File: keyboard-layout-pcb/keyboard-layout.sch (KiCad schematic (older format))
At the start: 33 parts, among them J1 Conn_01x06, J2 Conn_01x02, J3 Conn_01x02, Q1 IRLB871, U1 TSOP384xx, U2 TSMP58000, U3 RFM9xLoRa

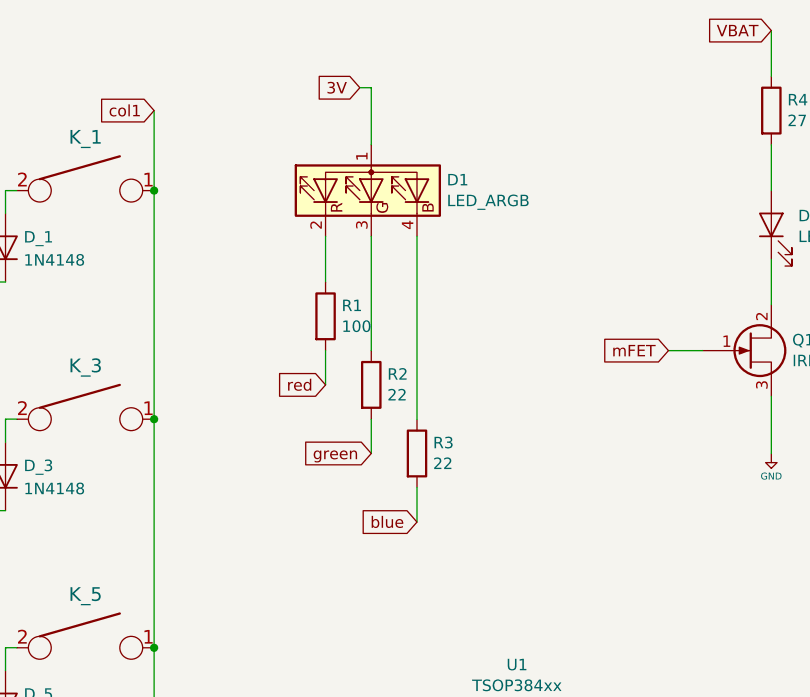
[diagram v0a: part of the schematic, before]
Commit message: Updated scematic to releft current operation
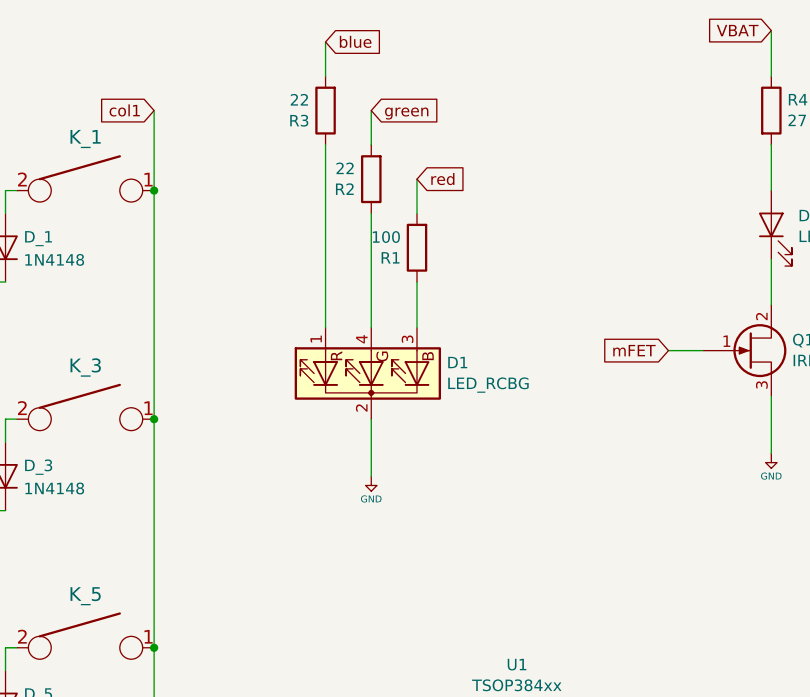
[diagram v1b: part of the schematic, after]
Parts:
- removed D1: LED_ARGB, LEDs:LED_D5.0mm-4, symbol Device:LED_ARGB
- added D1: LED_RCBG, LED_THT:LED_D5.0mm-4_RGB, symbol Device:LED_RCBG
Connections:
- net +5V: now also D1.2 (K)
- net at R1.1: now also D1.3 (BA)
- net at R2.1: now also D1.4 (GA)
- net at R3.1: now also D1.1 (RA)
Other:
- moved on the sheet: R1, R2, R3
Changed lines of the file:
@@
 	5250 5500 5400 5500
-$Comp
-L Device:LED_ARGB D1
-U 1 1 5DB4EFC4
-P 4250 2000
-F 0 "D1" V 4296 1670 50  0000 R CNN
-F 1 "LED_ARGB" V 4205 1670 50  0000 R CNN
-F 2 "LEDs:LED_D5.0mm-4" H 4250 1950 50  0001 C CNN
-F 3 "~" H 4250 1950 50  0001 C CNN
-	1    4250 2000
-	0    -1   -1   0
-$EndComp
 $Comp
 L Device:R R1
 U 1 1 5DB5148C
-P 4050 2550
-F 0 "R1" H 4120 2596 50  0000 L CNN
-F 1 "100" H 4120 2505 50  0000 L CNN
-F 2 "Resistors_THT:R_Axial_DIN0411_L9.9mm_D3.6mm_P12.70mm_Horizontal" V 3980 2550 50  0001 C CNN
-F 3 "~" H 4050 2550 50  0001 C CNN
-	1    4050 2550
-	1    0    0    -1
+P 4450 2250
+F 0 "R1" H 4520 2296 50  0000 L CNN
+F 1 "100" H 4520 2205 50  0000 L CNN
+F 2 "Resistors_THT:R_Axial_DIN0411_L9.9mm_D3.6mm_P12.70mm_Horizontal" V 4380 2250 50  0001 C CNN
+F 3 "~" H 4450 2250 50  0001 C CNN
+	1    4450 2250
+	-1   0    0    1
 $EndComp
 $Comp
 L Device:R R2
 U 1 1 5DB51AFC
-P 4250 2850
-F 0 "R2" H 4320 2896 50  0000 L CNN
-F 1 "22" H 4320 2805 50  0000 L CNN
-F 2 "Resistors_THT:R_Axial_DIN0411_L9.9mm_D3.6mm_P12.70mm_Horizontal" V 4180 2850 50  0001 C CNN
-F 3 "~" H 4250 2850 50  0001 C CNN
-	1    4250 2850
-	1    0    0    -1
+P 4250 1950
+F 0 "R2" H 4320 1996 50  0000 L CNN
+F 1 "22" H 4320 1905 50  0000 L CNN
+F 2 "Resistors_THT:R_Axial_DIN0411_L9.9mm_D3.6mm_P12.70mm_Horizontal" V 4180 1950 50  0001 C CNN
+F 3 "~" H 4250 1950 50  0001 C CNN
+	1    4250 1950
+	-1   0    0    1
 $EndComp
 $Comp
 L Device:R R3
 U 1 1 5DB51F49
-P 4450 3150
-F 0 "R3" H 4520 3196 50  0000 L CNN
-F 1 "22" H 4520 3105 50  0000 L CNN
-F 2 "Resistors_THT:R_Axial_DIN0411_L9.9mm_D3.6mm_P12.70mm_Horizontal" V 4380 3150 50  0001 C CNN
-F 3 "~" H 4450 3150 50  0001 C CNN
-	1    4450 3150
-	1    0    0    -1
-$EndComp
-Text GLabel 4050 2850 0    50   Input ~ 0
+P 4050 1650
+F 0 "R3" H 4120 1696 50  0000 L CNN
+F 1 "22" H 4120 1605 50  0000 L CNN
+F 2 "Resistors_THT:R_Axial_DIN0411_L9.9mm_D3.6mm_P12.70mm_Horizontal" V 3980 1650 50  0001 C CNN
+F 3 "~" H 4050 1650 50  0001 C CNN
+	1    4050 1650
+	-1   0    0    1
+$EndComp
+Text GLabel 4450 1950 2    50   Input ~ 0
 red
-Text GLabel 4250 3150 0    50   Input ~ 0
+Text GLabel 4250 1650 2    50   Input ~ 0
 green
-Text GLabel 4450 3450 0    50   Input ~ 0
+Text GLabel 4050 1350 2    50   Input ~ 0
 blue
 Wire Wire Line
-	4050 2400 4050 2200
-Wire Wire Line
-	4250 2200 4250 2700
-Wire Wire Line
-	4450 2200 4450 3000
-Wire Wire Line
-	4250 3000 4250 3150
-Wire Wire Line
-	4050 2700 4050 2850
-Wire Wire Line
-	4450 3300 4450 3450
+	4450 2400 4450 2600
+Wire Wire Line
+	4250 2600 4250 2100
+Wire Wire Line
+	4050 2600 4050 1800
+Wire Wire Line
+	4250 1800 4250 1650
+Wire Wire Line
+	4450 2100 4450 1950
+Wire Wire Line
+	4050 1500 4050 1350
 Text GLabel 7950 2950 0    50   Input ~ 0
 row0
@@
 Wire Wire Line
 	7950 2650 8100 2650
-Text GLabel 4200 1550 0    50   Input ~ 0
-3V
-Wire Wire Line
-	4200 1550 4250 1550
-Wire Wire Line
-	4250 1550 4250 1800
+Wire Wire Line
+	4250 3250 4250 3000
 Text GLabel 5400 5300 2    50   Input ~ 0
 3V
@@
 Wire Wire Line
 	5450 4300 5300 4300
+$Comp
+L keyboard_parts:GND #PWR01
+U 1 1 5DEEC9A8
+P 4250 3250
+F 0 "#PWR01" H 4250 3300 20  0001 C CNN
+F 1 "GND" H 4250 3150 30  0000 C CNN
+F 2 "" H 4250 3250 60  0000 C CNN
+F 3 "" H 4250 3250 60  0000 C CNN
+	1    4250 3250
+	1    0    0    -1
+$EndComp
+$Comp
+L Device:LED_RCBG D1
+U 1 1 5DEFA295
+P 4250 2800
+F 0 "D1" V 4296 2470 50  0000 R CNN
+F 1 "LED_RCBG" V 4205 2470 50  0000 R CNN
+F 2 "LED_THT:LED_D5.0mm-4_RGB" H 4250 2750 50  0001 C CNN
+F 3 "~" H 4250 2750 50  0001 C CNN
+	1    4250 2800
+	0    -1   -1   0
+$EndComp
 $EndSCHEMATC

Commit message: Revert "Updated scematic to releft current operation"
This reverts commit bc39922ebd05a59e5cfd160ddaddfcfa669e5cef.
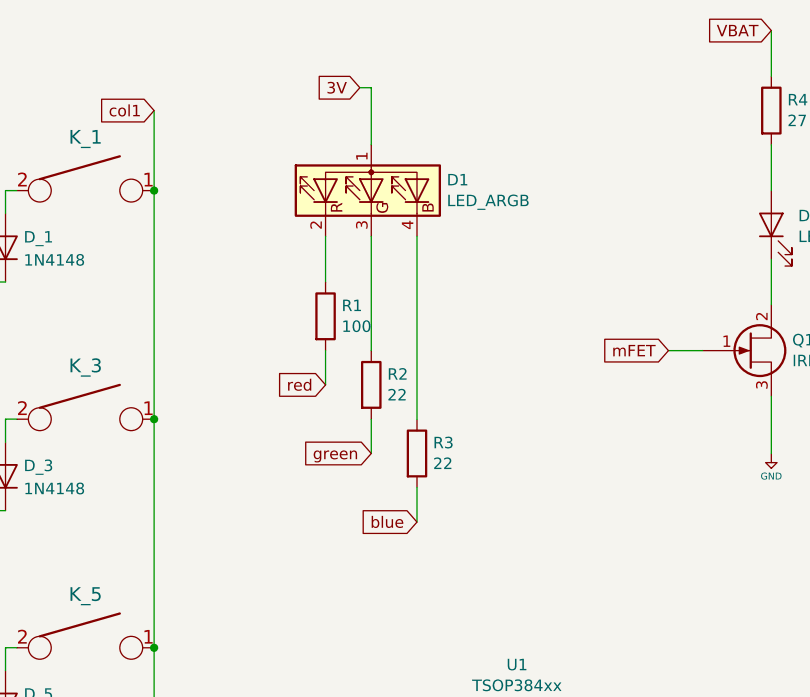
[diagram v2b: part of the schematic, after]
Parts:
- removed D1: LED_RCBG, LED_THT:LED_D5.0mm-4_RGB, symbol Device:LED_RCBG
- added D1: LED_ARGB, LEDs:LED_D5.0mm-4, symbol Device:LED_ARGB
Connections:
- net 3V: now also D1.1 (A)
- net at R1.1: now also D1.2 (RK)
- net at R2.1: now also D1.3 (GK)
- net at R3.1: now also D1.4 (BK)
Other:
- moved on the sheet: R1, R2, R3
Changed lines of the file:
@@
 	5250 5500 5400 5500
+$Comp
+L Device:LED_ARGB D1
+U 1 1 5DB4EFC4
+P 4250 2000
+F 0 "D1" V 4296 1670 50  0000 R CNN
+F 1 "LED_ARGB" V 4205 1670 50  0000 R CNN
+F 2 "LEDs:LED_D5.0mm-4" H 4250 1950 50  0001 C CNN
+F 3 "~" H 4250 1950 50  0001 C CNN
+	1    4250 2000
+	0    -1   -1   0
+$EndComp
 $Comp
 L Device:R R1
 U 1 1 5DB5148C
-P 4450 2250
-F 0 "R1" H 4520 2296 50  0000 L CNN
-F 1 "100" H 4520 2205 50  0000 L CNN
-F 2 "Resistors_THT:R_Axial_DIN0411_L9.9mm_D3.6mm_P12.70mm_Horizontal" V 4380 2250 50  0001 C CNN
-F 3 "~" H 4450 2250 50  0001 C CNN
-	1    4450 2250
-	-1   0    0    1
+P 4050 2550
+F 0 "R1" H 4120 2596 50  0000 L CNN
+F 1 "100" H 4120 2505 50  0000 L CNN
+F 2 "Resistors_THT:R_Axial_DIN0411_L9.9mm_D3.6mm_P12.70mm_Horizontal" V 3980 2550 50  0001 C CNN
+F 3 "~" H 4050 2550 50  0001 C CNN
+	1    4050 2550
+	1    0    0    -1
 $EndComp
 $Comp
 L Device:R R2
 U 1 1 5DB51AFC
-P 4250 1950
-F 0 "R2" H 4320 1996 50  0000 L CNN
-F 1 "22" H 4320 1905 50  0000 L CNN
-F 2 "Resistors_THT:R_Axial_DIN0411_L9.9mm_D3.6mm_P12.70mm_Horizontal" V 4180 1950 50  0001 C CNN
-F 3 "~" H 4250 1950 50  0001 C CNN
-	1    4250 1950
-	-1   0    0    1
+P 4250 2850
+F 0 "R2" H 4320 2896 50  0000 L CNN
+F 1 "22" H 4320 2805 50  0000 L CNN
+F 2 "Resistors_THT:R_Axial_DIN0411_L9.9mm_D3.6mm_P12.70mm_Horizontal" V 4180 2850 50  0001 C CNN
+F 3 "~" H 4250 2850 50  0001 C CNN
+	1    4250 2850
+	1    0    0    -1
 $EndComp
 $Comp
 L Device:R R3
 U 1 1 5DB51F49
-P 4050 1650
-F 0 "R3" H 4120 1696 50  0000 L CNN
-F 1 "22" H 4120 1605 50  0000 L CNN
-F 2 "Resistors_THT:R_Axial_DIN0411_L9.9mm_D3.6mm_P12.70mm_Horizontal" V 3980 1650 50  0001 C CNN
-F 3 "~" H 4050 1650 50  0001 C CNN
-	1    4050 1650
-	-1   0    0    1
-$EndComp
-Text GLabel 4450 1950 2    50   Input ~ 0
+P 4450 3150
+F 0 "R3" H 4520 3196 50  0000 L CNN
+F 1 "22" H 4520 3105 50  0000 L CNN
+F 2 "Resistors_THT:R_Axial_DIN0411_L9.9mm_D3.6mm_P12.70mm_Horizontal" V 4380 3150 50  0001 C CNN
+F 3 "~" H 4450 3150 50  0001 C CNN
+	1    4450 3150
+	1    0    0    -1
+$EndComp
+Text GLabel 4050 2850 0    50   Input ~ 0
 red
-Text GLabel 4250 1650 2    50   Input ~ 0
+Text GLabel 4250 3150 0    50   Input ~ 0
 green
-Text GLabel 4050 1350 2    50   Input ~ 0
+Text GLabel 4450 3450 0    50   Input ~ 0
 blue
 Wire Wire Line
-	4450 2400 4450 2600
-Wire Wire Line
-	4250 2600 4250 2100
-Wire Wire Line
-	4050 2600 4050 1800
-Wire Wire Line
-	4250 1800 4250 1650
-Wire Wire Line
-	4450 2100 4450 1950
-Wire Wire Line
-	4050 1500 4050 1350
+	4050 2400 4050 2200
+Wire Wire Line
+	4250 2200 4250 2700
+Wire Wire Line
+	4450 2200 4450 3000
+Wire Wire Line
+	4250 3000 4250 3150
+Wire Wire Line
+	4050 2700 4050 2850
+Wire Wire Line
+	4450 3300 4450 3450
 Text GLabel 7950 2950 0    50   Input ~ 0
 row0
@@
 Wire Wire Line
 	7950 2650 8100 2650
-Wire Wire Line
-	4250 3250 4250 3000
+Text GLabel 4200 1550 0    50   Input ~ 0
+3V
+Wire Wire Line
+	4200 1550 4250 1550
+Wire Wire Line
+	4250 1550 4250 1800
 Text GLabel 5400 5300 2    50   Input ~ 0
 3V
@@
 Wire Wire Line
 	5450 4300 5300 4300
-$Comp
-L keyboard_parts:GND #PWR01
-U 1 1 5DEEC9A8
-P 4250 3250
-F 0 "#PWR01" H 4250 3300 20  0001 C CNN
-F 1 "GND" H 4250 3150 30  0000 C CNN
-F 2 "" H 4250 3250 60  0000 C CNN
-F 3 "" H 4250 3250 60  0000 C CNN
-	1    4250 3250
-	1    0    0    -1
-$EndComp
-$Comp
-L Device:LED_RCBG D1
-U 1 1 5DEFA295
-P 4250 2800
-F 0 "D1" V 4296 2470 50  0000 R CNN
-F 1 "LED_RCBG" V 4205 2470 50  0000 R CNN
-F 2 "LED_THT:LED_D5.0mm-4_RGB" H 4250 2750 50  0001 C CNN
-F 3 "~" H 4250 2750 50  0001 C CNN
-	1    4250 2800
-	0    -1   -1   0
-$EndComp
 $EndSCHEMATC
